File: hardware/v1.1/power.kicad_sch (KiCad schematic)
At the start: 38 parts, among them U1 ECP5U_12_CABGA256, U2 TLV62569DBV, U3 TLV62569DBV, U4 TLV62569DBV, Y1 SITxxxxxx-1x-33E-50.000000

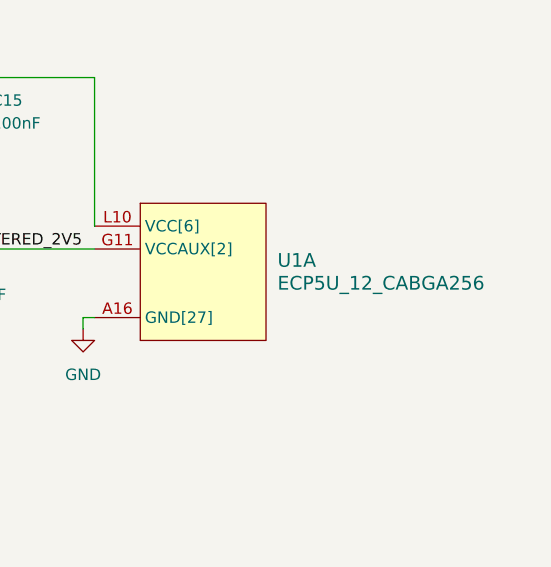
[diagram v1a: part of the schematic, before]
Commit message: Clean up the design by a bit
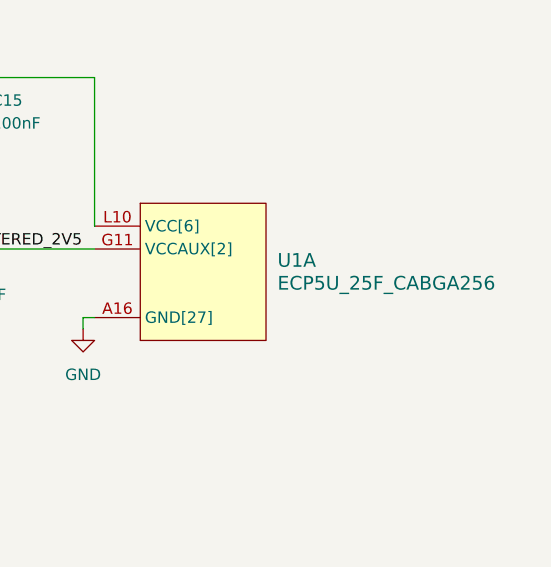
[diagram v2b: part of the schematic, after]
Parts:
- U1: value ECP5U_12_CABGA256 -> ECP5U_25F_CABGA256
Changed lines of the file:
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@@
 			)
 		)
-		(property "Value" "ECP5U_12_CABGA256"
+		(property "Value" "ECP5U_25F_CABGA256"
 			(at 247.65 74.9299 0)
 			(effects

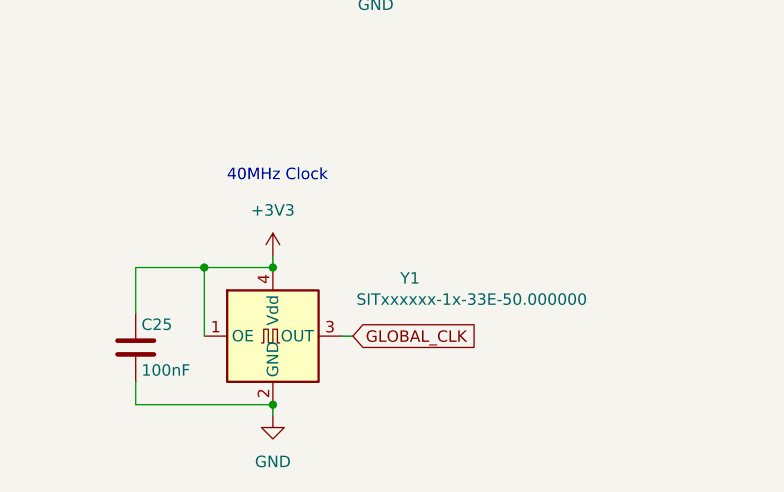
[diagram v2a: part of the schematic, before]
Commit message: Fix wrong dates on shematic and pcb sheet
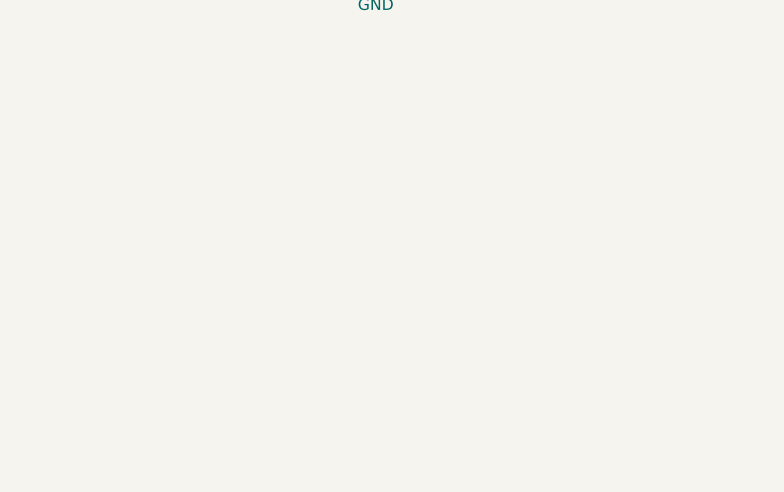
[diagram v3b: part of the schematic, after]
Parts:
- removed C25: 100nF, Capacitor_SMD:C_0402_1005Metric, symbol Device:C
- removed Y1: SITxxxxxx-1x-33E-50.000000, Oscillator:Oscillator_SMD_SiT_PQFN-4Pin_2.5x2.0mm, symbol Oscillator:SiT8008xx-1x-xxE
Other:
- note removed: "40MHz Clock"

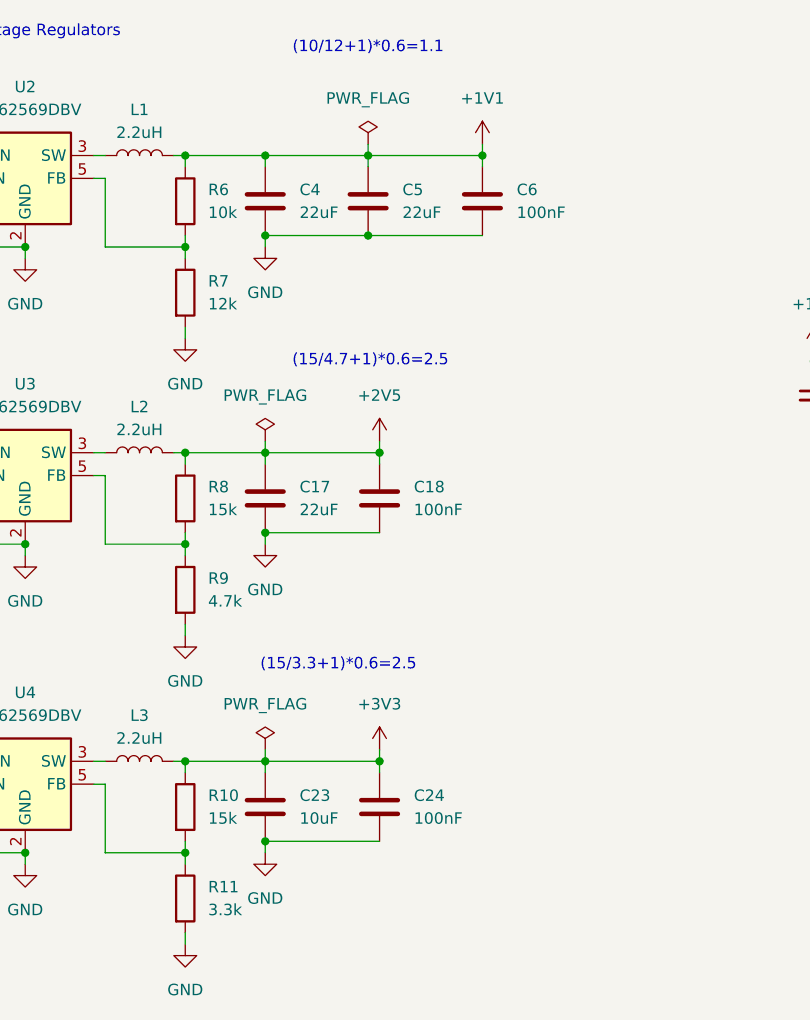
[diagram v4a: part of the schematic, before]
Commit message: Fix wrong comment text
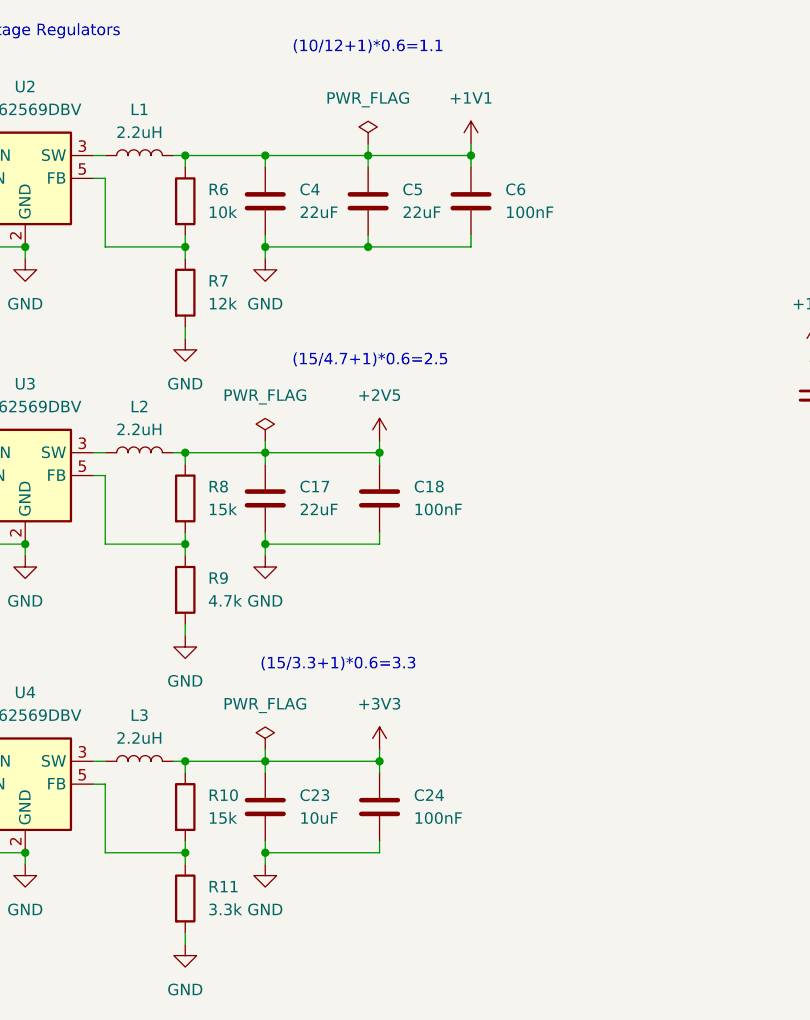
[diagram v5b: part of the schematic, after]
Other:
- note added: "(15/3.3+1)*0.6=3.3"
- note removed: "(15/3.3+1)*0.6=2.5"
- moved on the sheet: C6
